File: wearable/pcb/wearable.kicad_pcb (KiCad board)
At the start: 4 copper layers, 28 x 39.2 mm, 81 parts, among them J1 USB_C_Receptacle_USB2.0, J2 Extension, J3 Extension, U1 BC833, U10 TCR3UFxxA, U11 TMP1075, U2 MCP73832-2-OT, U3 S-85S1A, U4 LIS2DE12, U5 APDS-9250, U6 MX25R8035FZxxx0, U7 PCF85063ATL, U8 DT1446-04V, U9 MAX30102, Y71 32.768kHz

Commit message: Work out the fabrication layers.
Signed-off-by: Mike M. Volokhov <mike.volokhov@gmail.com>
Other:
- board text added: "— NO PANEL MOUNTS ON THIS SIDE —"
- board text removed: "PANEL MOUNT POINT"

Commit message: The bill of materials has been completed.
While working on the BoM, fix error in the battery sensing circuit.
The R23 must be 6.8M or bigger (previously was 4M). This is required
to keep the ADC voltage below VDD=2.5V value.

Signed-off-by: Mike M. Volokhov <mike.volokhov@gmail.com>
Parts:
- C13, C14: value Tuning -> Tune
- C2: value 100nF/200V -> 100nF/100V
- R1, R2, R22, R3: value R_US -> Tune
- R21: value R_US -> 10k
- R23: value 4M -> 6.8M

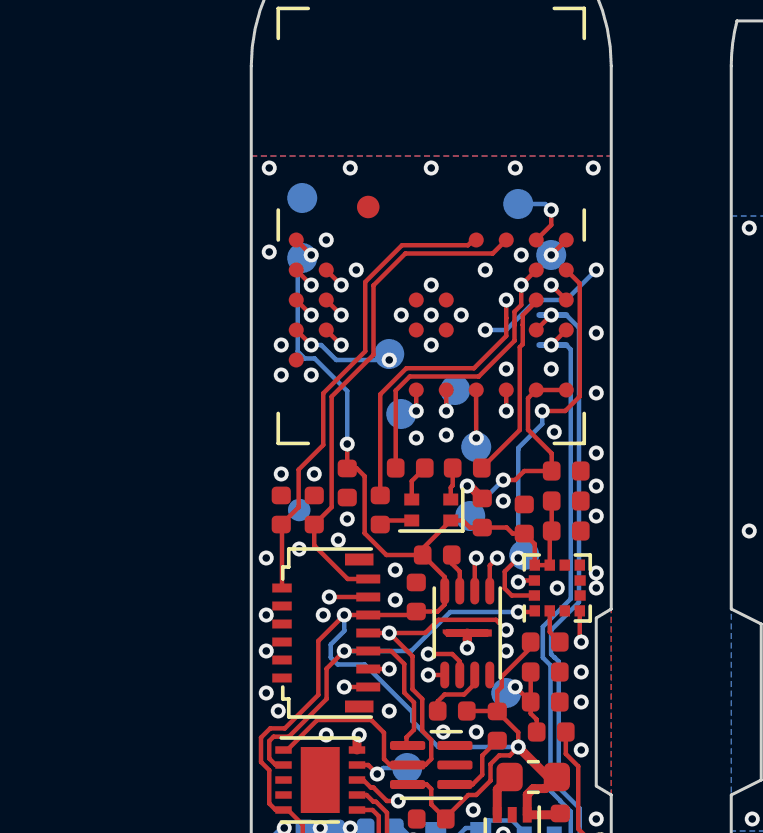
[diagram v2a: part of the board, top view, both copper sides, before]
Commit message: Nordic Review: make ground area on the top layer solid.
To acheive this, route NFC traces on the bottom size, make the
BC833M pad connection to zones solid, and move some test points
across the board.

Also, temporarily remove the front fiducial from the core board.
It will be placed later when the boards will get panelized.

Signed-off-by: Mike M. Volokhov <mike.volokhov@gmail.com>
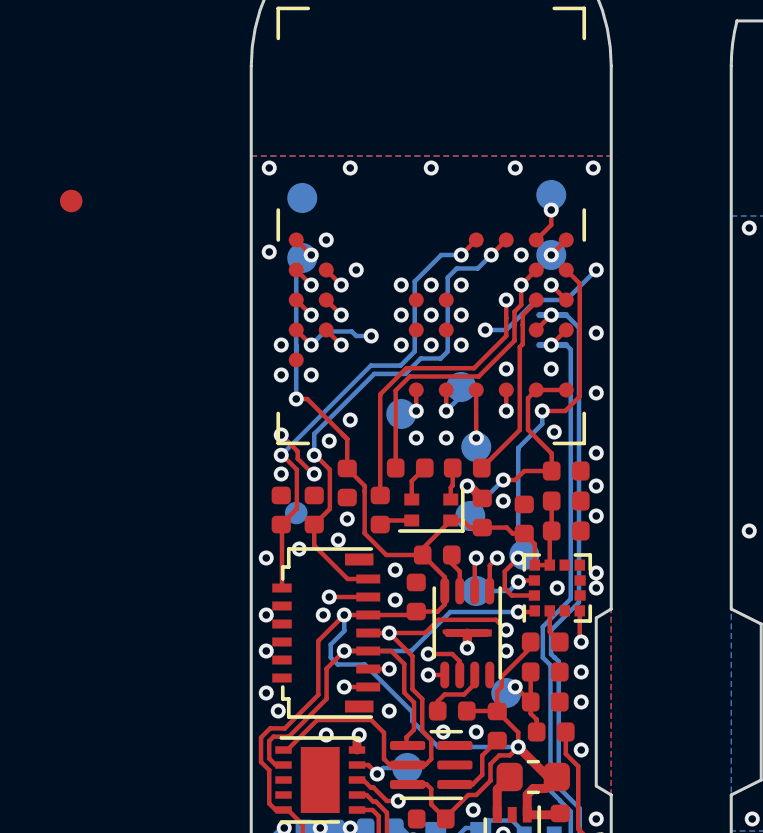
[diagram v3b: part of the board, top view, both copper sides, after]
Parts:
- moved FID1 9.90 mm to (138.0, 90.0)
- moved TP42 8.42 mm to (151.5, 103.0)
- moved TP12 1.14 mm to (154.0, 89.8)
- moved TP15 0.22 mm to (151.0, 96.2)
- moved FID2 0.14 mm to (145.5, 100.4)
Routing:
- net /Core Board/ACC_INT2: track 14.6 -> 16.9 mm
- net GND: track 15.4 -> 17.2 mm, vias 67 -> 73
- net /Core Board/SWDCLK: track 2.39 -> 1.49 mm
- net /Core Board/NFC1: track 16.8 -> 17.0 mm, vias 0 -> 2
- net /Core Board/NFC2: vias 0 -> 2

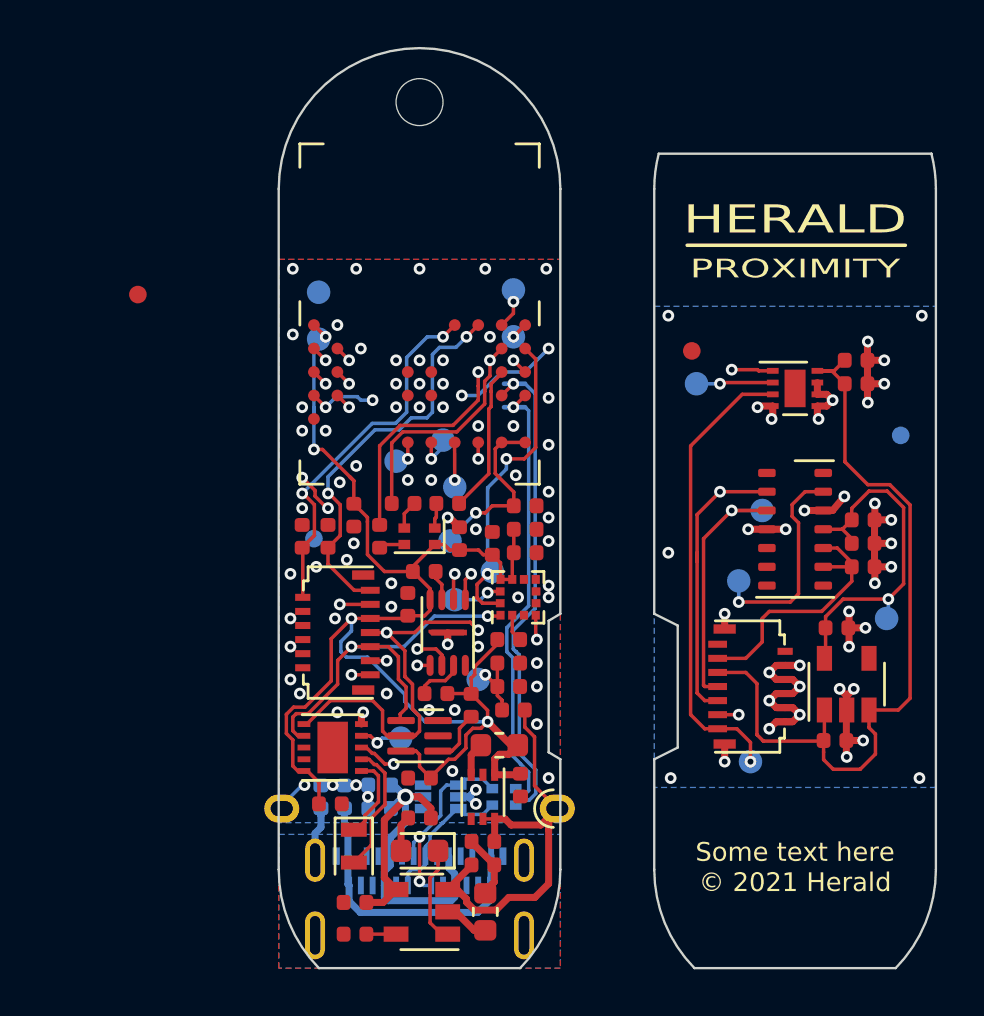
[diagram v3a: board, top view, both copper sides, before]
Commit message: Completely rework the temperature sensor layout.
Now, use a dedicated thermal guide to the IC exposed pad, and
decouple the sensor from the rest of the board.

Signed-off-by: Mike M. Volokhov <mike.volokhov@gmail.com>
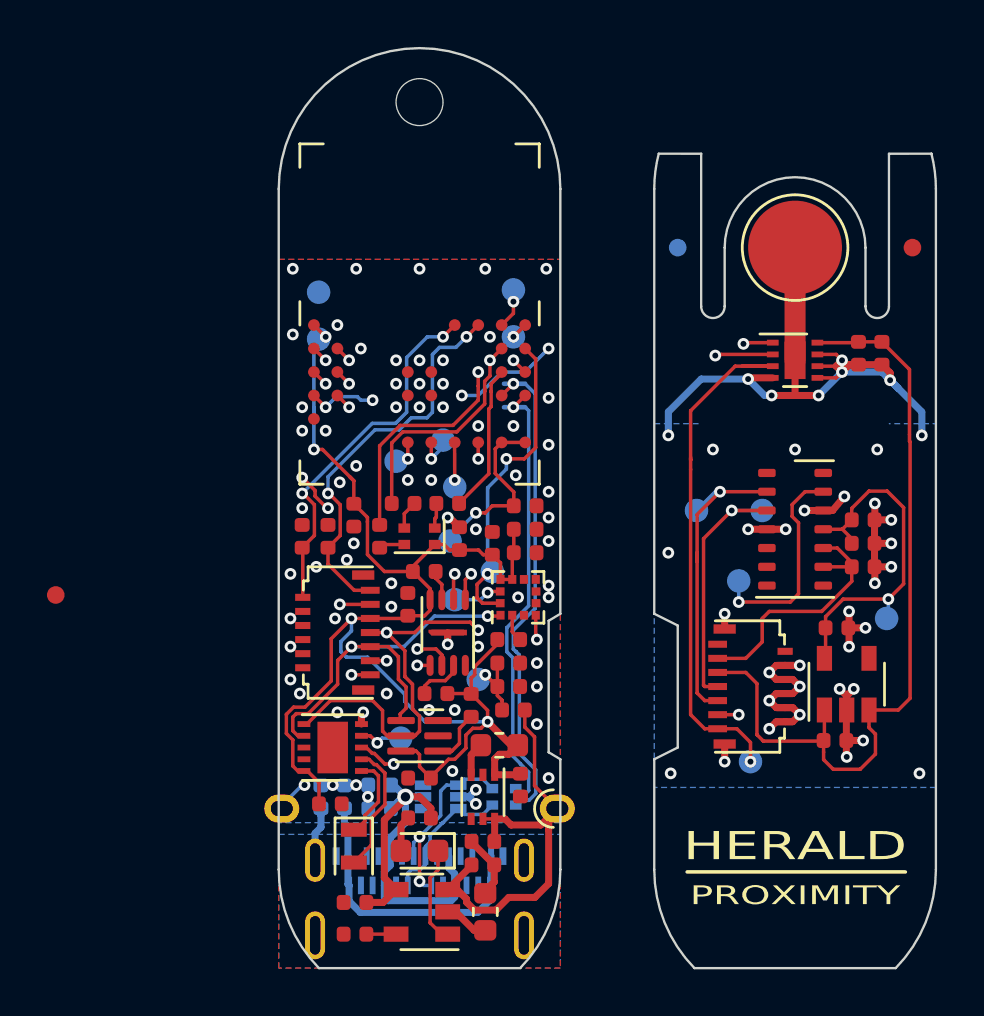
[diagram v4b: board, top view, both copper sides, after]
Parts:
- added H2: ThermalSlot, Herald_Extras:MillSlot_8.0x1.0mm, F.Cu at (166.0, 95.5)
- added TP112: ThPad, TestPoint:TestPoint_Pad_D4.0mm, F.Cu at (166.0, 88.0)
- moved FID1 13.3 mm to (134.5, 102.8)
- moved FID4 12.4 mm to (161.0, 88.0)
- moved FID3 10.4 mm to (171.0, 88.0)
- moved FID2 8.54 mm to (146.3, 108.9)
- moved TP5 5.40 mm to (161.8, 99.2)
- moved C112 1.70 mm to (169.7, 92.5), turned to 90 degrees
- moved U11 1.20 mm to (166.0, 92.8)
- moved C111 0.32 mm to (168.7, 92.5), turned to 90 degrees
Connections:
- U11 pad 9: (no net) -> GND1
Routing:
- net GND1: track 32.4 -> 55.2 mm, vias 37 -> 38
- net /Extension Board/SCL: track 20.2 -> 23.2 mm
- net /Extension Board/TMP_INT: track 19.7 -> 22.5 mm
- net /Extension Board/SDA: track 19.5 -> 21.9 mm
- net VDD1: track 33.6 -> 34.2 mm
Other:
- outline, holes or cut-outs redrawn

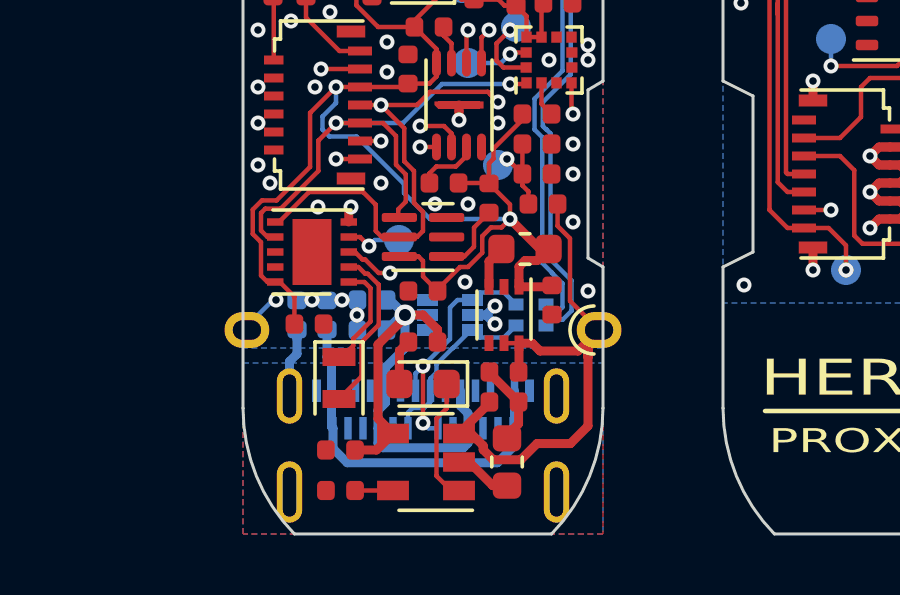
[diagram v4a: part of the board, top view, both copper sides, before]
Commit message: Make pcbnew DRC happy.
This improves pad-to-pad clearance for the SOT-563 packages,
and allows overlapping footprints (yep, real estate is expenisve).

Signed-off-by: Mike M. Volokhov <mike.volokhov@gmail.com>
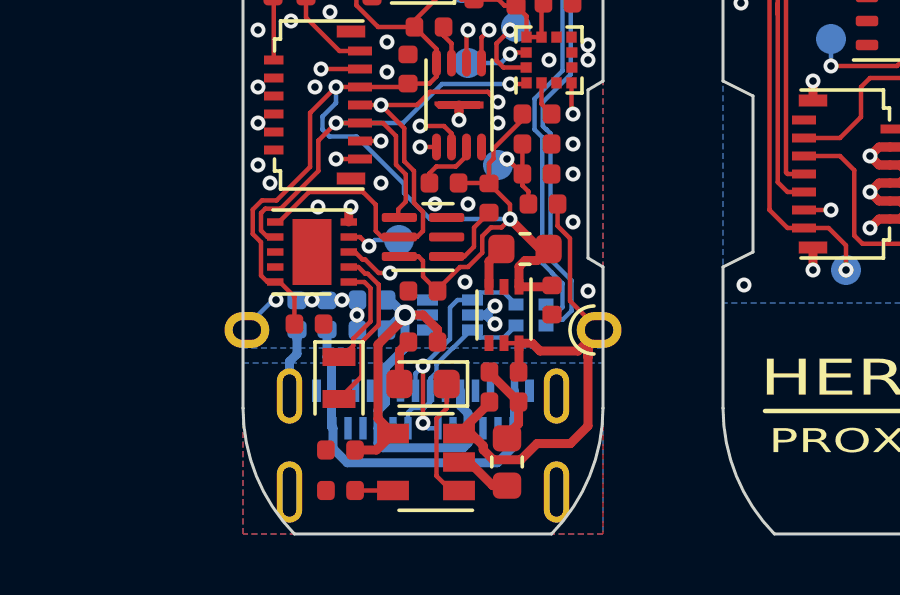
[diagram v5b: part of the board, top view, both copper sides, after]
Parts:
- U8: footprint Package_TO_SOT_SMD:SOT-563 -> Herald_Extras:SOT-563
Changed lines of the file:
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@@
     (add_net GNDPWR)
+  )
+  (module Herald_Extras:SOT-563 (layer B.Cu)
+    (at 150.9 111.4 180)
+    (descr "SOT563, 5 mils pad-to-pad clearance")
+    (tags SOT-563)
+    (attr smd)
+    (fp_text reference U8 (at 0 1.7) (layer B.SilkS) hide
+      (effects (font (size 1 1) (thickness 0.15)) (justify mirror))
+    )
+    (fp_text value DT1446-04V (at -1 0.6 90) (layer B.Fab)
+      (effects (font (size 0.4 0.4) (thickness 0.06)) (justify mirror))
+    )
+    (fp_text user %R (at 0 0 270) (layer B.Fab)
+      (effects (font (size 0.4 0.4) (thickness 0.0625)) (justify mirror))
+    )
+    (fp_line (start -0.65 0.5) (end -0.3 0.85) (layer B.Fab) (width 0.1))
+    (fp_line (start 0.65 -0.9) (end -0.65 -0.9) (layer B.SilkS) (width 0.12))
+    (fp_line (start -0.9 0.9) (end 0.65 0.9) (layer B.SilkS) (width 0.12))
+    (fp_line (start -0.65 0.5) (end -0.65 -0.85) (layer B.Fab) (width 0.1))
+    (fp_line (start -0.65 -0.85) (end 0.65 -0.85) (layer B.Fab) (width 0.1))
+    (fp_line (start 0.65 -0.85) (end 0.65 0.85) (layer B.Fab) (width 0.1))
+    (fp_line (start 0.65 0.85) (end -0.3 0.85) (layer B.Fab) (width 0.1))
+    (fp_line (start -1.35 1.1) (end 1.35 1.1) (layer B.CrtYd) (width 0.05))
+    (fp_line (start -1.35 1.1) (end -1.35 -1.1) (layer B.CrtYd) (width 0.05))
+    (fp_line (start 1.35 -1.1) (end 1.35 1.1) (layer B.CrtYd) (width 0.05))
+    (fp_line (start 1.35 -1.1) (end -1.35 -1.1) (layer B.CrtYd) (width 0.05))
+    (pad 5 smd rect (at 0.75 0 180) (size 0.7 0.375) (layers B.Cu B.Paste B.Mask)
+      (net 1 VBUS))
+    (pad 4 smd rect (at 0.75 -0.5 180) (size 0.7 0.375) (layers B.Cu B.Paste B.Mask)
+      (net 49 "Net-(U8-Pad4)"))
+    (pad 2 smd rect (at -0.75 0 180) (size 0.7 0.375) (layers B.Cu B.Paste B.Mask)
+      (net 2 GND))
+    (pad 6 smd rect (at 0.75 0.5 180) (size 0.7 0.375) (layers B.Cu B.Paste B.Mask)
+      (net 50 "Net-(U8-Pad6)"))
+    (pad 3 smd rect (at -0.75 -0.5 180) (size 0.7 0.375) (layers B.Cu B.Paste B.Mask)
+      (net 16 "Net-(J1-PadA6)"))
+    (pad 1 smd rect (at -0.75 0.5 180) (size 0.7 0.375) (layers B.Cu B.Paste B.Mask)
+      (net 15 "Net-(J1-PadA7)"))
+    (model ${KISYS3DMOD}/Package_TO_SOT_SMD.3dshapes/SOT-563.wrl
+      (at (xyz 0 0 0))
+      (scale (xyz 1 1 1))
+      (rotate (xyz 0 0 0))
+    )
   )
   (module Herald_Extras:MillSlot_8.0x1.0mm (layer F.Cu)
@@
       (effects (font (size 1 1) (thickness 0.15)) (justify mirror))
     )
-    (fp_text value 120R/0.6A (at 2.3 0 90) (layer B.Fab)
+    (fp_text value 120R/0.6A (at 1.1 0.6 90) (layer B.Fab)
       (effects (font (size 0.4 0.4) (thickness 0.06)) (justify mirror))
     )
@@
       (effects (font (size 1 1) (thickness 0.15)) (justify mirror))
     )
-    (fp_text value 120R/0.6A (at 2.3 0 90) (layer B.Fab)
+    (fp_text value 120R/0.6A (at 1.1 -0.6 90) (layer B.Fab)
       (effects (font (size 0.4 0.4) (thickness 0.06)) (justify mirror))
     )
@@
       (effects (font (size 1 1) (thickness 0.15)) (justify mirror))
     )
-    (fp_text value Fiducial (at 0 1.1) (layer B.Fab)
+    (fp_text value Fiducial (at 0 -2.1 90) (layer B.Fab)
       (effects (font (size 0.4 0.4) (thickness 0.06)) (justify mirror))
     )
     (fp_circle (center 0 0) (end 0.75 0) (layer B.Fab) (width 0.1))
     (fp_circle (center 0 0) (end 1 0) (layer B.CrtYd) (width 0.05))
-    (fp_text user %R (at 0 0) (layer B.Fab)
+    (fp_text user %R (at 0 0 90) (layer B.Fab)
       (effects (font (size 0.3 0.3) (thickness 0.05)) (justify mirror))
     )
@@
       (scale (xyz 1 1 1))
       (rotate (xyz 0 0 90))
-    )
-  )
-  (module Package_TO_SOT_SMD:SOT-563 (layer B.Cu)
-    (at 150.9 111.4 180)
-    (descr SOT563)
-    (tags SOT-563)
-    (attr smd)
-    (fp_text reference U8 (at 0 1.7) (layer B.SilkS) hide
-      (effects (font (size 1 1) (thickness 0.15)) (justify mirror))
-    )
-    (fp_text value DT1446-04V (at 0 3 90) (layer B.Fab)
-      (effects (font (size 0.4 0.4) (thickness 0.06)) (justify mirror))
-    )
-    (fp_line (start -0.65 0.5) (end -0.3 0.85) (layer B.Fab) (width 0.1))
-    (fp_line (start 0.65 -0.9) (end -0.65 -0.9) (layer B.SilkS) (width 0.12))
-    (fp_line (start -0.9 0.9) (end 0.65 0.9) (layer B.SilkS) (width 0.12))
-    (fp_line (start -0.65 0.5) (end -0.65 -0.85) (layer B.Fab) (width 0.1))
-    (fp_line (start -0.65 -0.85) (end 0.65 -0.85) (layer B.Fab) (width 0.1))
-    (fp_line (start 0.65 -0.85) (end 0.65 0.85) (layer B.Fab) (width 0.1))
-    (fp_line (start 0.65 0.85) (end -0.3 0.85) (layer B.Fab) (width 0.1))
-    (fp_line (start -1.35 1.1) (end 1.35 1.1) (layer B.CrtYd) (width 0.05))
-    (fp_line (start -1.35 1.1) (end -1.35 -1.1) (layer B.CrtYd) (width 0.05))
-    (fp_line (start 1.35 -1.1) (end 1.35 1.1) (layer B.CrtYd) (width 0.05))
-    (fp_line (start 1.35 -1.1) (end -1.35 -1.1) (layer B.CrtYd) (width 0.05))
-    (fp_text user %R (at 0 0 270) (layer B.Fab)
-      (effects (font (size 0.4 0.4) (thickness 0.0625)) (justify mirror))
-    )
-    (pad 5 smd rect (at 0.75 0 180) (size 0.7 0.4) (layers B.Cu B.Paste B.Mask)
-      (net 1 VBUS))
-    (pad 4 smd rect (at 0.75 -0.5 180) (size 0.7 0.4) (layers B.Cu B.Paste B.Mask)
-      (net 49 "Net-(U8-Pad4)"))
-    (pad 2 smd rect (at -0.75 0 180) (size 0.7 0.4) (layers B.Cu B.Paste B.Mask)
-      (net 2 GND))
-    (pad 6 smd rect (at 0.75 0.5 180) (size 0.7 0.4) (layers B.Cu B.Paste B.Mask)
-      (net 50 "Net-(U8-Pad6)"))
-    (pad 3 smd rect (at -0.75 -0.5 180) (size 0.7 0.4) (layers B.Cu B.Paste B.Mask)
-      (net 16 "Net-(J1-PadA6)"))
-    (pad 1 smd rect (at -0.75 0.5 180) (size 0.7 0.4) (layers B.Cu B.Paste B.Mask)
-      (net 15 "Net-(J1-PadA7)"))
-    (model ${KISYS3DMOD}/Package_TO_SOT_SMD.3dshapes/SOT-563.wrl
-      (at (xyz 0 0 0))
-      (scale (xyz 1 1 1))
-      (rotate (xyz 0 0 0))
     )
   )
@@
       (effects (font (size 1 1) (thickness 0.15)) (justify mirror))
     )
-    (fp_text value 4.7uF (at 0 -0.6) (layer B.Fab)
-      (effects (font (size 0.4 0.4) (thickness 0.06)) (justify mirror))
-    )
+    (fp_text value 4.7uF (at 0.4 -0.6) (layer B.Fab)
+      (effects (font (size 0.4 0.4) (thickness 0.06)) (justify mirror))
+    )
